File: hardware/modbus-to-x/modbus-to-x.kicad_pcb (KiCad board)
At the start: 2 copper layers, 38 parts, among them J1 PWR, J2 UART, SW1 SW_Push, SW2 SW_Push, U1 AMS1117-3.3, U3 MAX3485, U4 ESP32-WROOM-32D, U5 AT24CS64-XHM, U6 AT24CS64-XHM, U7 LMR14020SQDPRTQ1

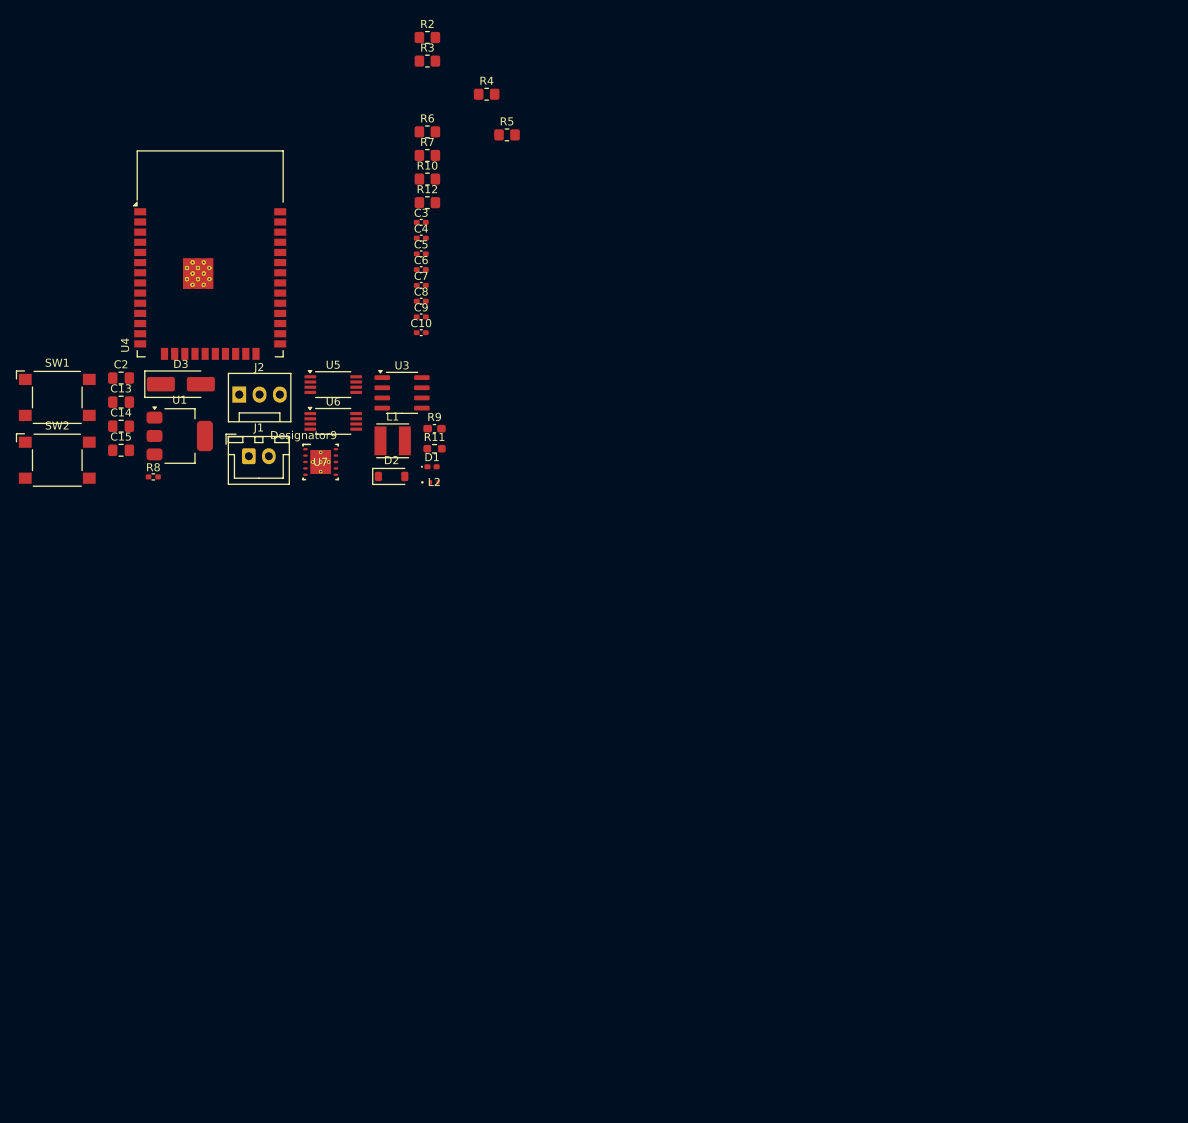
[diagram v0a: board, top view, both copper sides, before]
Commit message: updated footprints
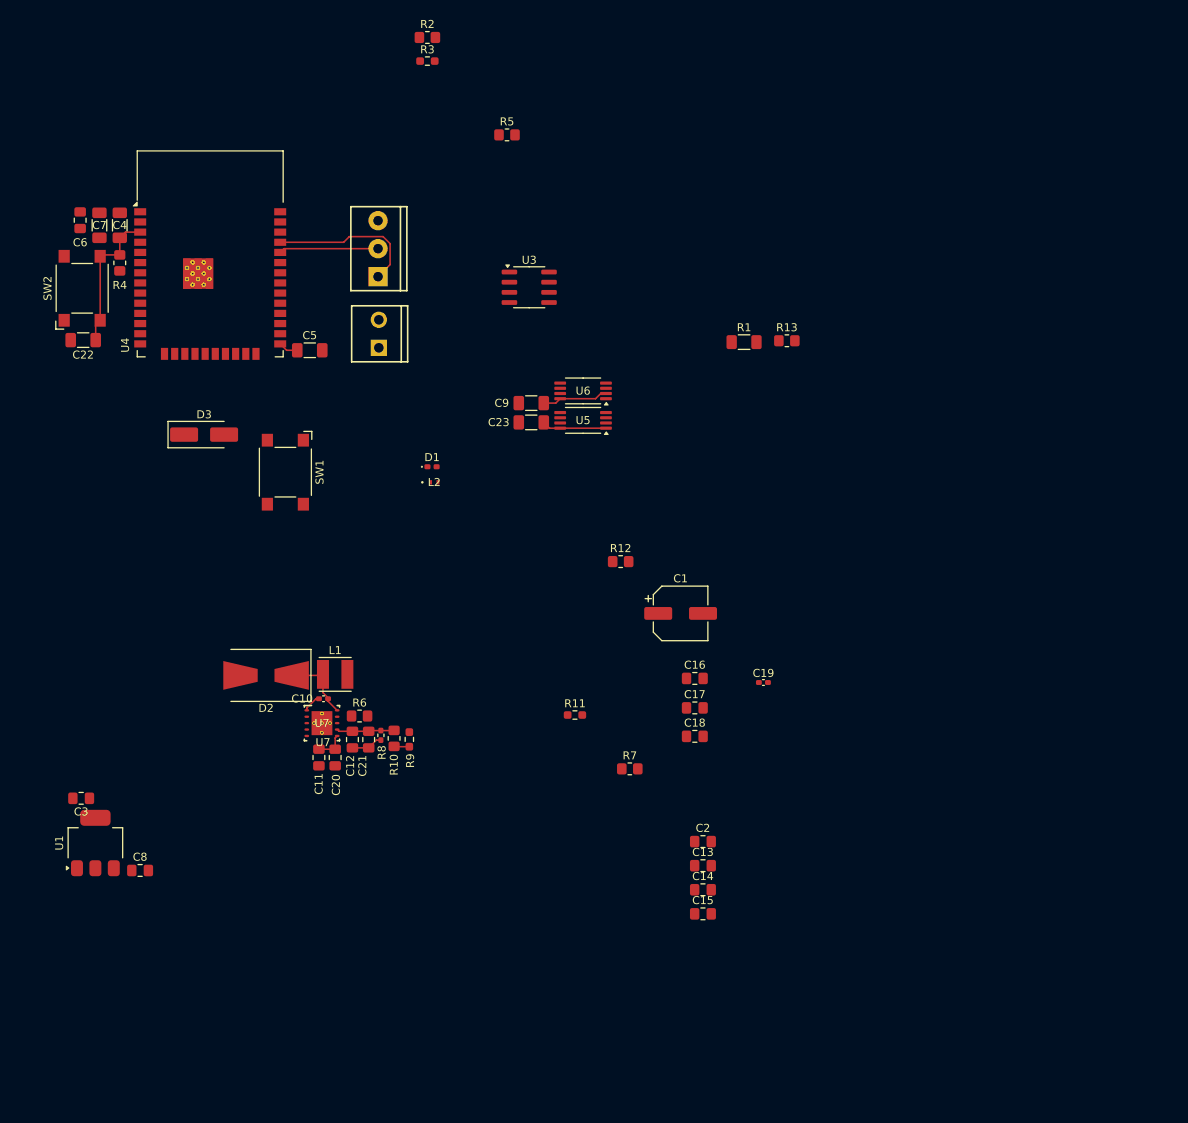
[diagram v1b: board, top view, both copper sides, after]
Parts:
- added C1: 47uF, Capacitor_SMD:CP_Elec_6.3x5.4, F.Cu at (96.9, 85.2)
- added C11: 2.2nF, Capacitor_SMD:C_0805_2012Metric_Pad1.18x1.45mm_HandSolder, F.Cu at (51.7, 103.2)
- added C12: 100pF, Capacitor_SMD:C_0805_2012Metric_Pad1.18x1.45mm_HandSolder, F.Cu at (55.9, 101.0)
- added C16: 10uF, Capacitor_SMD:C_0805_2012Metric_Pad1.18x1.45mm_HandSolder, F.Cu at (98.7, 93.3)
- added C17: 10uF, Capacitor_SMD:C_0805_2012Metric_Pad1.18x1.45mm_HandSolder, F.Cu at (98.7, 97.0)
- added C18: 10uF, Capacitor_SMD:C_0805_2012Metric_Pad1.18x1.45mm_HandSolder, F.Cu at (98.7, 100.6)
- added C19: 0.01uF, Capacitor_SMD:C_0402_1005Metric_Pad0.74x0.62mm_HandSolder, F.Cu at (107.3, 93.9)
- added C20: 2.2nF, Capacitor_SMD:C_0805_2012Metric_Pad1.18x1.45mm_HandSolder, F.Cu at (53.7, 103.2)
- added C21: 100pF, Capacitor_SMD:C_0805_2012Metric_Pad1.18x1.45mm_HandSolder, F.Cu at (57.9, 101.0)
- added C22: 0.1uF, Capacitor_SMD:C_1206_3216Metric_Pad1.33x1.80mm_HandSolder, F.Cu at (22.2, 51.1)
- added C23: 0.1uF, Capacitor_SMD:C_1206_3216Metric_Pad1.33x1.80mm_HandSolder, F.Cu at (78.2, 61.3)
- added R1: 100R, Resistor_SMD:R_1206_3216Metric_Pad1.30x1.75mm_HandSolder, F.Cu at (104.8, 51.3)
- added R13: 10K, Resistor_SMD:R_0805_2012Metric_Pad1.20x1.40mm_HandSolder, F.Cu at (110.2, 51.1)
- C3: value 0.1uF/50V(10%) -> 22uF; footprint Capacitor_SMD:C_0402_1005Metric_Pad0.74x0.62mm_HandSolder -> Capacitor_SMD:C_0805_2012Metric_Pad1.18x1.45mm_HandSolder
- C4, C5, C7: value 0.1uF/50V(10%) -> 0.1uF; footprint Capacitor_SMD:C_0402_1005Metric_Pad0.74x0.62mm_HandSolder -> Capacitor_SMD:C_1206_3216Metric_Pad1.33x1.80mm_HandSolder
- C6, C8: value 22uF/10V(20%) -> 22uF; footprint Capacitor_SMD:C_0402_1005Metric_Pad0.74x0.62mm_HandSolder -> Capacitor_SMD:C_0805_2012Metric_Pad1.18x1.45mm_HandSolder
- C9: value 22uF/10V(20%) -> 0.1uF; footprint Capacitor_SMD:C_0402_1005Metric_Pad0.74x0.62mm_HandSolder -> Capacitor_SMD:C_1206_3216Metric_Pad1.33x1.80mm_HandSolder
- D2: value MBR0530 -> MBRS340T3G; footprint Diode_SMD:D_SOD-123 -> Diode_SMD:D_SMB-SMC_Universal_Handsoldering
- J1: footprint Connector_JST:JST_XH_B2B-XH-A_1x02_P2.50mm_Vertical -> SparkFun-Connector:Screw_Terminal_3.5mm-2
- J2: footprint Connector:FanPinHeader_1x03_P2.54mm_Vertical -> SparkFun-Connector:Screw_Terminal_3.5mm-3
- R3: footprint Resistor_SMD:R_0805_2012Metric_Pad1.20x1.40mm_HandSolder -> Resistor_SMD:R_0603_1608Metric_Pad0.98x0.95mm_HandSolder
- R9: footprint Capacitor_SMD:C_0603_1608Metric_Pad1.08x0.95mm_HandSolder -> Resistor_SMD:R_0603_1608Metric_Pad0.98x0.95mm_HandSolder
- moved C13 93.0 mm to (99.7, 116.8)
- moved C14 93.0 mm to (99.7, 119.8)
- moved C15 93.0 mm to (99.7, 122.8)
- moved C2 93.0 mm to (99.7, 113.7)
- moved C3 83.6 mm to (22.0, 108.3), turned to 180 degrees
- moved R7 80.7 mm to (90.6, 104.6)
- moved C8 79.4 mm to (29.3, 117.3)
- moved R6 73.5 mm to (56.8, 98.0)
- moved R10 70.0 mm to (61.1, 100.8), turned to 90 degrees
- moved U1 52.0 mm to (23.7, 113.9), turned to 90 degrees
- moved R12 51.0 mm to (89.4, 78.7)
- moved R4 50.5 mm to (26.8, 41.4), turned to 90 degrees
- moved C10 47.4 mm to (52.3, 95.9), turned to 180 degrees
- moved C6 43.1 mm to (21.8, 36.1), turned to -90 degrees
- moved R8 43.0 mm to (59.4, 100.5), turned to 90 degrees
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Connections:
- C3 pad 1: GND -> VDD33
- C3 pad 2: /EN -> GND
- C4 pad 1: GND -> /EN
- C4 pad 2: /IO_0 -> GND
- C5 pad 1: GND -> /IO_0
- C5 pad 2: /EN -> GND
- R4 pad 2: SDA_BUS -> /EN
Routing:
- net /TX_0: track 0.00 -> 19.1 mm
- net /EN: track 0.00 -> 18.2 mm
- net VDD33: track 0.00 -> 16.3 mm
- net /RX_0: track 0.00 -> 12.4 mm
- net Net-(D2-K): track 0.00 -> 9.19 mm
- net Net-(U7-FB): track 0.00 -> 7.25 mm
- net VCC5: track 0.00 -> 3.96 mm
- net Net-(U7-SS): track 0.00 -> 3.79 mm
- net /IO_0: track 0.00 -> 2.46 mm
- net Net-(U7-BOOT): track 0.00 -> 2.30 mm
- net Net-(R10-Pad1): track 0.00 -> 1.92 mm

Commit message: hardware tweaks
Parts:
- removed L2: MPZ1005S121CT000, MPZ1005S121CT000:IND_1005_TDK-L
- removed U4: ESP32-WROOM-32D, RF_Module:ESP32-WROOM-32D
- added C24: 22uF, Capacitor_SMD:C_0805_2012Metric_Pad1.18x1.45mm_HandSolder, F.Cu at (99.0, 85.8)
- added C25: 0.1uF, Capacitor_SMD:C_1206_3216Metric_Pad1.33x1.80mm_HandSolder, F.Cu at (98.4, 88.1)
- added J3: Screw_Terminal_3.5mm_2, SparkFun-Connector:Screw_Terminal_3.5mm-2, F.Cu at (104.0, 121.4)
- added R14: 620R, Resistor_SMD:R_0805_2012Metric_Pad1.20x1.40mm_HandSolder, F.Cu at (115.2, 122.2)
- added R15: 10K, Resistor_SMD:R_0805_2012Metric_Pad1.20x1.40mm_HandSolder, F.Cu at (88.1, 146.1)
- added U2: ESP32-WROOM-32DM113DH6400PH3Q0, ESP32-WROOM-32D-M113DH6400PH3Q0:ESP32-WROOM-32DM113DH6400PH3Q0_EXP, F.Cu at (110.5, 94.1)
- C22: value 0.1uF -> 1uF; footprint Capacitor_SMD:C_1206_3216Metric_Pad1.33x1.80mm_HandSolder -> Nichicon UMA1H010MCD2TP:CAP_UMA_3X5_NCH
- C6: value 22uF -> 0.1uF; footprint Capacitor_SMD:C_0805_2012Metric_Pad1.18x1.45mm_HandSolder -> Capacitor_SMD:C_1206_3216Metric_Pad1.33x1.80mm_HandSolder
- R1: value 100R -> 120R
- R2: value 10K -> 620R
- SW1, SW2: value SW_Push -> 1825910-7; footprint Button_Switch_SMD:SW_SPST_Omron_B3FS-105xP -> digikey-footprints:Switch_Tactile_SMD_6x6mm_PTS645
- moved C7 130.0 mm to (120.1, 124.6), turned to 0 degrees
- moved C22 123.9 mm to (119.7, 127.5), turned to 0 degrees
- moved R2 117.0 mm to (115.2, 119.0)
- moved R3 110.3 mm to (101.3, 120.4), turned to 90 degrees
- moved D3 100.5 mm to (126.7, 108.8), turned to -90 degrees
- moved R5 94.3 mm to (118.7, 109.1), turned to -90 degrees
- moved C4 91.9 mm to (99.8, 92.6), turned to -90 degrees
- moved U3 87.7 mm to (121.3, 120.7), turned to 180 degrees
- moved R4 86.0 mm to (96.9, 91.3), turned to -90 degrees
- moved SW2 84.4 mm to (91.9, 92.1)
- moved J1 80.1 mm to (124.4, 98.4), turned to -90 degrees
- moved J2 78.8 mm to (124.4, 87.1), turned to -90 degrees
- moved C6 78.6 mm to (79.5, 89.5), turned to 90 degrees
- moved C3 75.6 mm to (97.0, 99.2), turned to -90 degrees
- moved U1 69.6 mm to (92.3, 101.7)
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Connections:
- net /MB_INT_B renamed /RS485-
- net SCL_BUS renamed /SCL_BUS
- net SDA_BUS renamed /SDA_BUS
- C22 pad 1: /EN -> VDD33
- C5 pad 1: /IO_0 -> Net-(C5-Pad1)
- C5 pad 2: GND -> Net-(C5-Pad2)
- C6 pad 1: GND -> Net-(C6-Pad1)
- C6 pad 2: VDD33 -> Net-(C6-Pad2)
- C7 pad 1: GND -> VDD33
- C7 pad 2: VDD33 -> GND
- D3 pad 1: Net-(D3-A1) -> /VBUS_12
- J1 pad 1: Net-(D3-A1) -> /VBUS_12
- R1 pad 1: /MB_INT_A -> /RS485+
- R2 pad 1: VDD33 -> /RS485+
- R2 pad 2: /EN -> VDD33
- SW1 pad 1: GND -> Net-(C5-Pad2)
- SW1 pad 2: /IO_0 -> GND
- SW2 pad 1: GND -> Net-(C6-Pad2)
- SW2 pad 2: /EN -> GND
- U3 pad 1: /RX_2 -> /RX_{2}
- U3 pad 2: /RS485_RE -> /RS485_DE_RE
- U3 pad 3: /RS485_DE -> /RS485_DE_RE
- U3 pad 4: /TX_2 -> /TX_{2}
- U3 pad 6: /MB_INT_A -> /RS485+
- U7 pad V: (no net) -> GND
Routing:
- net GND: track 0.00 -> 96.6 mm, vias 0 -> 21
- net /VBUS_12: track 0.00 -> 54.6 mm
- net VDD33: track 16.3 -> 58.8 mm, vias 0 -> 14
- net /SDA_BUS: track 0.00 -> 40.8 mm, vias 0 -> 3
- net /SCL_BUS: track 0.00 -> 40.2 mm, vias 0 -> 3
- net /IO_0: track 2.46 -> 40.8 mm, vias 0 -> 2
- net VCC5: track 3.96 -> 32.9 mm, vias 0 -> 6
- net /PGOOD: track 0.00 -> 26.8 mm, vias 0 -> 2
- net /RX_{2}: track 0.00 -> 23.8 mm, vias 0 -> 2
- net /RS485_DE_RE: track 0.00 -> 22.0 mm, vias 0 -> 2
- net Net-(C6-Pad2): track 0.00 -> 21.3 mm
- net /TX_{2}: track 0.00 -> 20.3 mm, vias 0 -> 2
- net /RS485+: track 0.00 -> 19.2 mm
- net Net-(C6-Pad1): track 0.00 -> 16.8 mm
- net /RS485-: track 0.00 -> 15.1 mm
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- added copper zone on F.Cu, net /VBUS_12
- added copper zone on In2.Cu, net GND
- added copper zone on F.Cu, net Net-(D2-K)
- added copper zone on F.Cu, net VCC5
- added copper zone on In1.Cu, net VCC5
- added copper zone on In1.Cu, net VDD33
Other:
- board outline added: 53 x 53 mm
- copper layers 2 -> 4
- board text added: "9-16V"
- board text added: "A"
- board text added: "B"
- board text added: "BOOT"
- board text added: "C_ff"
- board text added: "C_in"
- board text added: "C_out"
- board text added: "C_ss"
- board text added: "GND"
- board text added: "GND TX RX"
- board text added: "RESET"
- board text added: "RS485"
- board text added: "R_fbb"
- board text added: "R_fbt"
- board text added: "R_rt"

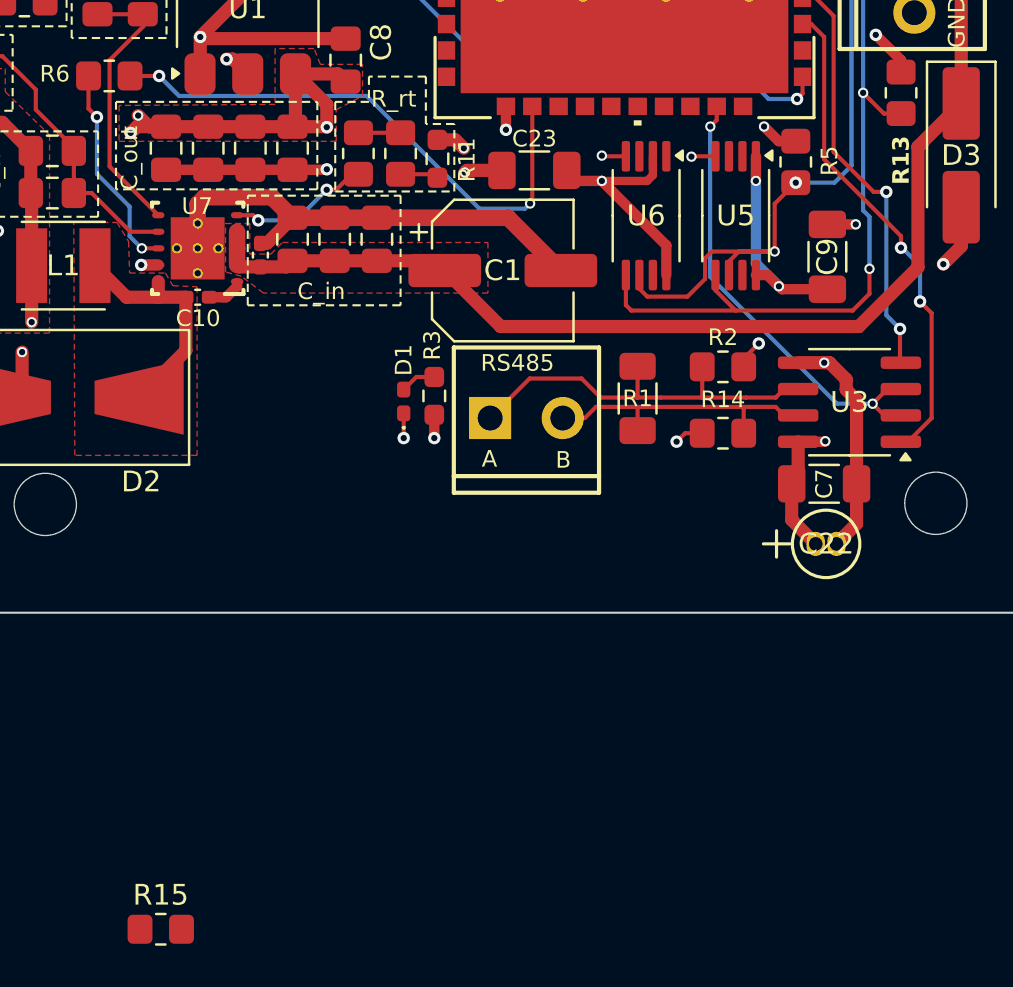
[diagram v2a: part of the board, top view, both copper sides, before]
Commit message: added bulk ecap to max485 ic
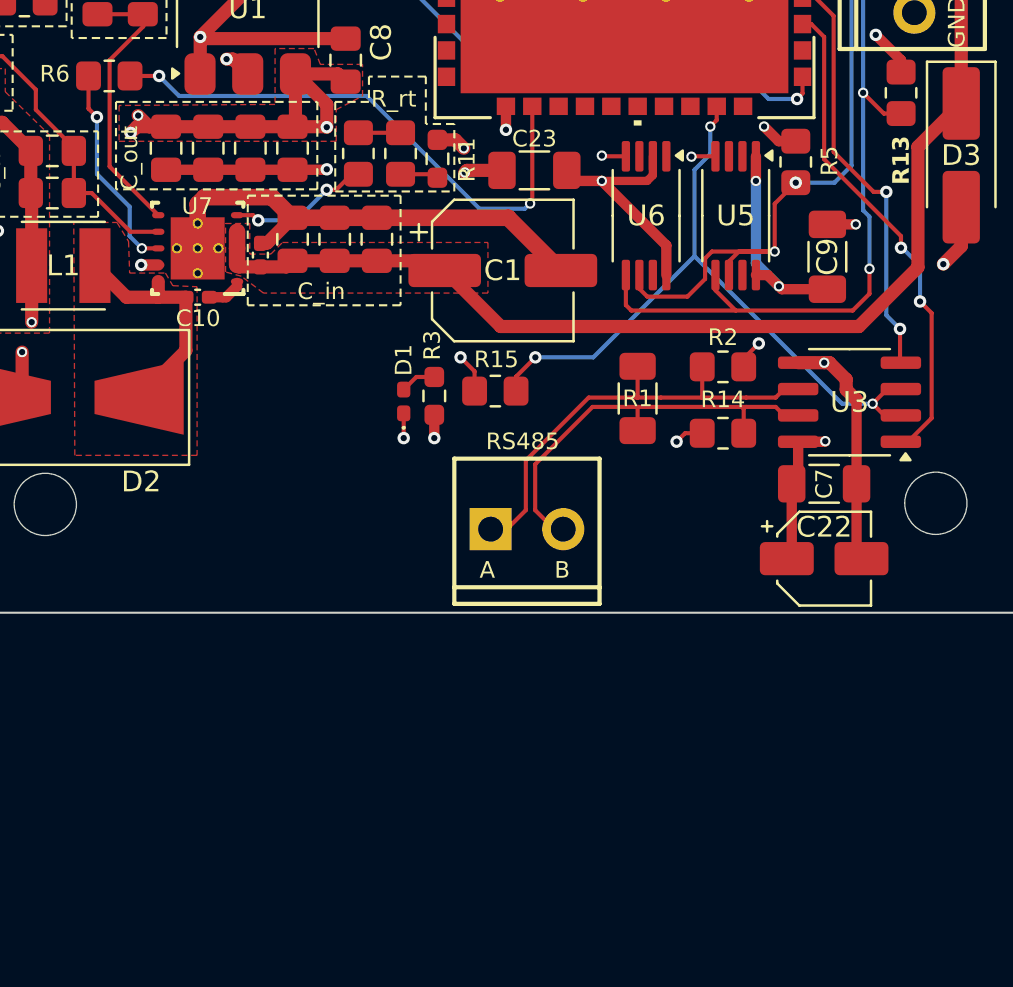
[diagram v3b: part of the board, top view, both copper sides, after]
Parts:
- C22: footprint Nichicon UMA1H010MCD2TP:CAP_UMA_3X5_NCH -> Capacitor_SMD:CP_Elec_4x5.4
- moved R15 30.5 mm to (104.2, 120.1)
- moved J3 5.36 mm to (104.0, 126.8)
- moved C22 0.82 mm to (120.1, 128.2)
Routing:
- net /RS485_DE_RE: track 22.0 -> 34.1 mm, vias 2 -> 3
- net /RS485-: track 15.1 -> 20.4 mm
- net /RS485+: track 19.2 -> 22.0 mm
- net VDD33: track 58.8 -> 61.0 mm, vias 14 -> 15

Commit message: status leds
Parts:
- added D4: LED, LED_SMD:LED_0402_1005Metric_Pad0.77x0.64mm_HandSolder, F.Cu at (93.8, 80.2)
- added D5: LED, LED_SMD:LED_0402_1005Metric_Pad0.77x0.64mm_HandSolder, F.Cu at (91.2, 80.2)
- added D6: LED, LED_SMD:LED_0402_1005Metric_Pad0.77x0.64mm_HandSolder, F.Cu at (88.8, 80.2)
- added R16: 2K, Resistor_SMD:R_0603_1608Metric_Pad0.98x0.95mm_HandSolder, F.Cu at (94.5, 82.7)
- added R17: 2K, Resistor_SMD:R_0603_1608Metric_Pad0.98x0.95mm_HandSolder, F.Cu at (91.8, 82.7)
- added R18: 2K, Resistor_SMD:R_0603_1608Metric_Pad0.98x0.95mm_HandSolder, F.Cu at (88.2, 82.6)
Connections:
- U2 pad 10: unconnected-(U2-IO25-Pad10) -> /STAT_2
- U2 pad 11: unconnected-(U2-IO26-Pad11) -> /STAT_3
- U2 pad 9: unconnected-(U2-IO33-Pad9) -> /STAT_1
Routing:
- net /STAT_3: track 0.00 -> 24.0 mm, vias 0 -> 2
- net /STAT_2: track 0.00 -> 21.0 mm, vias 0 -> 2
- net /STAT_1: track 0.00 -> 19.0 mm, vias 0 -> 2
- net GND: track 97.0 -> 103.4 mm, vias 21 -> 23
- net Net-(D4-A): track 0.00 -> 1.66 mm
- net Net-(D5-A): track 0.00 -> 1.62 mm
- net Net-(D6-A): track 0.00 -> 1.59 mm

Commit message: board cleanup
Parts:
- added G***: LOGO, Modbus To X Graphics:logo, B.Cu at (100.3, 111.7)
- moved R18 0.60 mm to (88.8, 82.6)
- moved D6 0.46 mm to (88.3, 80.2)
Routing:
- net /SCL_BUS: track 40.2 -> 37.4 mm, vias 3 -> 2
- net /STAT_3: track 24.0 -> 23.2 mm, vias 2 -> 0
- net GND: track 103.4 -> 102.7 mm
- net /STAT_1: track 19.0 -> 19.6 mm, vias 2 -> 0
- net /STAT_2: track 21.0 -> 20.8 mm, vias 2 -> 0

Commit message: added receptable
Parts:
- added J4: SSQ-110-X-X-D, Connector Receptable 2x10 20POS:SAMTEC_SSQ-110-X-X-D, F.Cu at (145.3, 113.6)

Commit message: improved edge cuts
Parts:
- added TP_RX2_TX2: TestPoint_2Pole, Connector_PinHeader_2.54mm:PinHeader_1x02_P2.54mm_Vertical, F.Cu at (131.6, 121.3)
- moved J4 51.6 mm to (96.2, 129.5)
- moved J3 10.9 mm to (114.3, 130.5)
- moved G*** 6.51 mm to (106.7, 110.6)
- moved D4 5.36 mm to (98.5, 82.7)
- moved D5 5.04 mm to (95.6, 82.7)
- moved R16 5.04 mm to (98.9, 85.2)
- moved R17 5.04 mm to (96.1, 85.2)
- moved R18 5.04 mm to (93.2, 85.2)
- moved D6 5.04 mm to (92.6, 82.7)
- moved C10 4.59 mm to (94.0, 117.7)
- moved C18 4.59 mm to (98.5, 114.9)
- moved C20 4.59 mm to (91.3, 103.0)
- moved C25 4.59 mm to (102.5, 90.2)
- moved C5 4.59 mm to (83.6, 96.6)
- moved D3 4.59 mm to (130.8, 110.9)
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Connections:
- J4 pad 04: /RS485_DE_RE -> unconnected-(J4-Pad04)
- J4 pad 07: /RX_{2} -> unconnected-(J4-Pad07)
- J4 pad 08: /TX_{2} -> unconnected-(J4-Pad08)
- J4 pad 12: unconnected-(J4-Pad12) -> /SPI_CS
- J4 pad 13: /RX_0 -> /SPI_MISO
- J4 pad 14: /TX_0 -> /SPI_CLK
- J4 pad 15: unconnected-(J4-Pad15) -> /SPI_MOSI
- J4 pad 17: unconnected-(J4-Pad17) -> /RS485_DE_RE
- U2 pad 29: unconnected-(U2-IO5-Pad29) -> /SPI_CS
- U2 pad 30: unconnected-(U2-IO18-Pad30) -> /SPI_CLK
- U2 pad 31: unconnected-(U2-IO19-Pad31) -> /SPI_MISO
- U2 pad 37: unconnected-(U2-IO23-Pad37) -> /SPI_MOSI
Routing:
- net /SPI_CS: track 0.00 -> 114.7 mm, vias 0 -> 1
- net /SPI_CLK: track 0.00 -> 107.3 mm, vias 0 -> 1
- net /SPI_MISO: track 0.00 -> 100.3 mm, vias 0 -> 1
- net /SPI_MOSI: track 0.00 -> 83.1 mm, vias 0 -> 1
- net VCC5: track 32.9 -> 73.5 mm
- net /SCL_BUS: track 37.4 -> 74.2 mm, vias 2 -> 3
- net /SDA_BUS: track 40.8 -> 69.9 mm, vias 3 -> 4
- net VDD33: track 61.0 -> 75.5 mm, vias 15 -> 16
- net /RS485_DE_RE: track 34.1 -> 48.1 mm
- net /VBUS_12: track 54.6 -> 66.7 mm
- net GND: track 102.7 -> 113.8 mm, vias 23 -> 26
- net /RX_{2}: track 23.8 -> 28.5 mm
- net /TX_{2}: track 20.3 -> 24.2 mm
- net /RS485-: track 20.4 -> 22.9 mm
- net /RS485+: track 22.0 -> 24.4 mm
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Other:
- board size 53 x 53 mm -> 55 x 55 mm
